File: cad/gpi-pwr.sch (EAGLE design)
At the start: 95 parts, among them CN1 HEADER-1X2, CN2 HEADER-3X1, CN3 HEADER-1X2.4, Q1 MOSFETTO247REV, Q3 MOSFETTO247REV, Q5 MOSFETTO247REV, Q6 MOSFETTO247REV, Q7 MOSFETTO247REV, Q8 MOSFETTO247REV, U1 ACS709, U2 ACS709, U3 ACPL-P346P346, U4 ACPL-P346P346, U5 ACPL-P346P346, U6 ACPL-P346P346, U7 ACPL-P346P346, U8 ACPL-P346P346

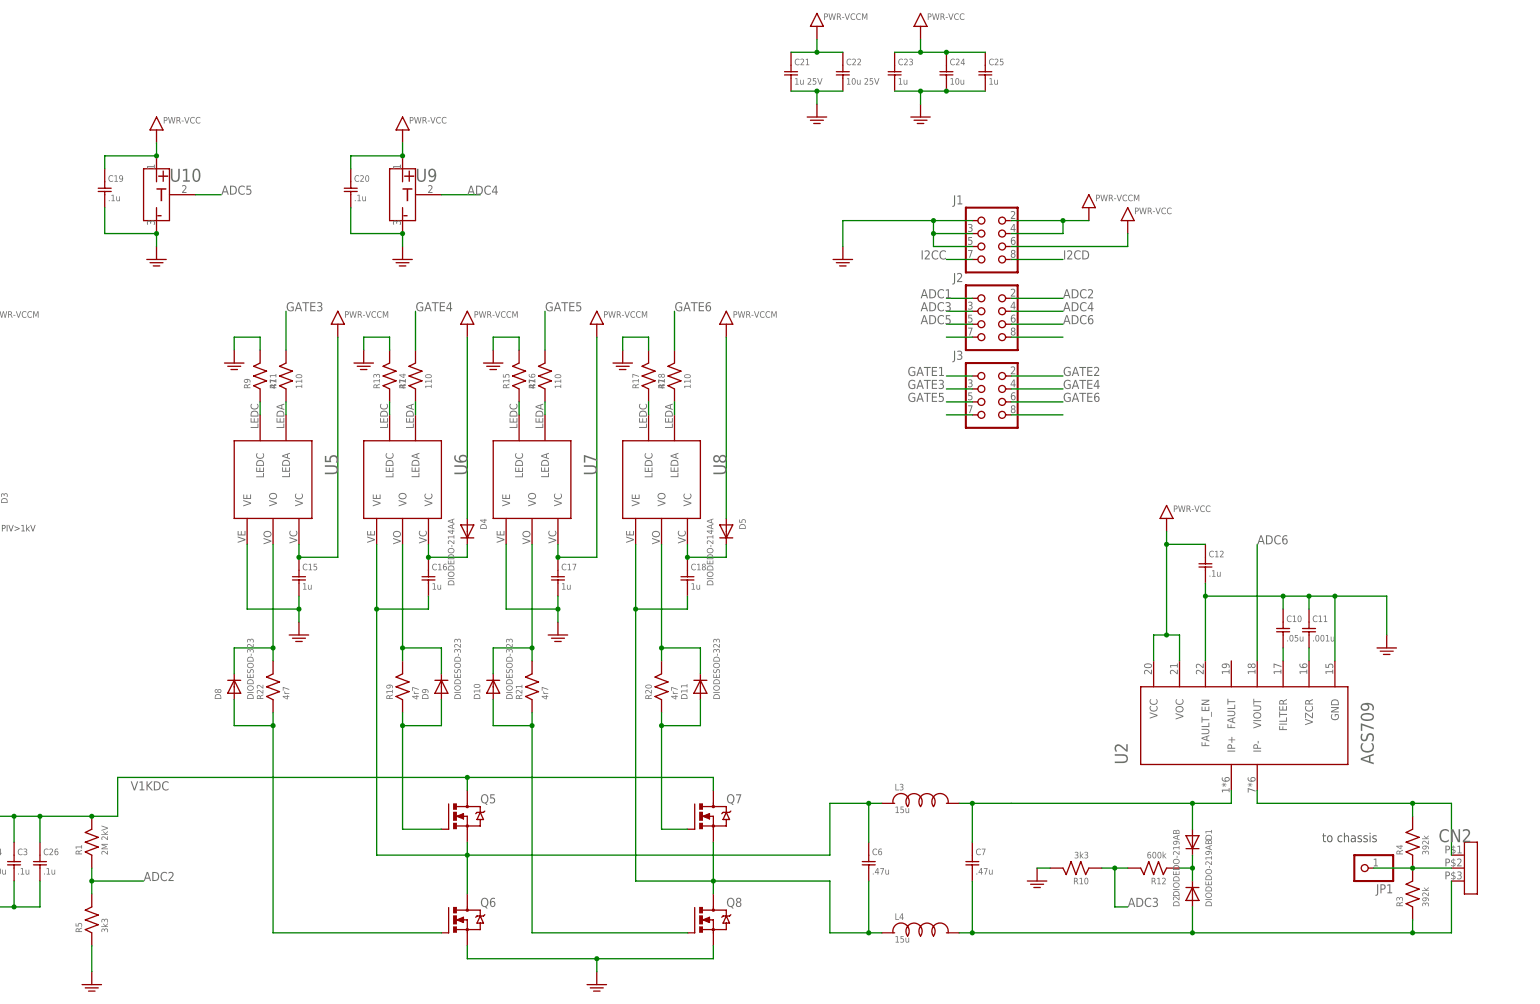
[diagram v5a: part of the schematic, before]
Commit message: op-amps on v-divs
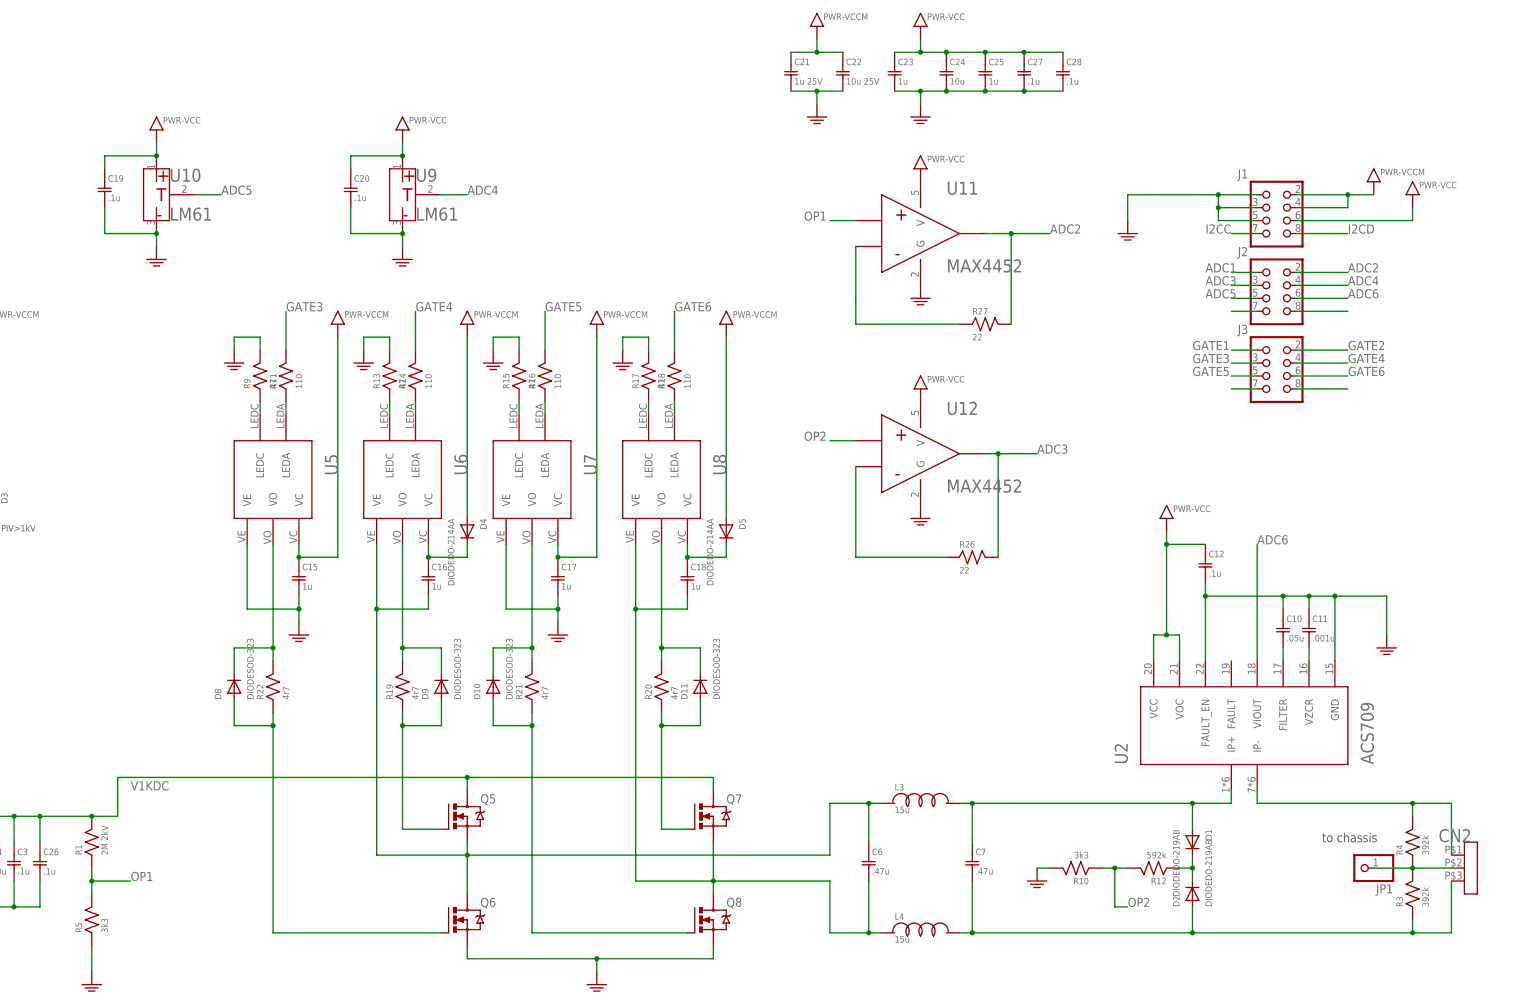
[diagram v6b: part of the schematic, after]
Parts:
- added C27, C28: .1u, jaw:C0603
- added R26, R27: 22, jaw:R0603
- added U11, U12: MAX4452, jaw:OPAMP
- R12: value 600k -> 592k
- U10, U9: value (none) -> LM61
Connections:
- new net N$51: R26.P$1, U12.INM
- new net N$52: R27.P$1, U11.INM
- new net OP1: R1.P$1, R5.P$2, U11.INP
- new net OP2: R10.P$1, R12.P$2, U12.INP
- net ADC2: now also R27.P$2, U11.OUT; no longer R1.P$1, R5.P$2
- net ADC3: now also R26.P$2, U12.OUT; no longer R10.P$1, R12.P$2
- net GND: now also C27.P$2, C28.P$2, U11.G, U12.G
- net VCC: now also C27.P$1, C28.P$1, U11.V, U12.V
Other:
- moved on the sheet: J1, J2, J3

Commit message: zoned grounds
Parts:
- added Z1: SHORT, jaw:SHORT
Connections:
- new net GNDA: C10.P$1, C11.P$1, C12.P$2, C19.P$2, C20.P$2, C23.P$2, C24.P$2, C25.P$2, C27.P$2, C28.P$2, C5.P$1, C8.P$1, C9.P$2, R10.P$2, R5.P$1, U1.FAULT_EN, U1.GND, U10.G, U11.G, U12.G, U2.FAULT_EN, U2.GND, U9.G, Z1.P$1
- new net GNDM: C13.P$2, C15.P$2, C17.P$2, C21.P$2, C22.P$2, J1.P$1, J1.P$3, J1.P$5, R13.P$2, R15.P$2, R17.P$2, R2.P$2, R7.P$2, R9.P$2, U3.VE, U5.VE, U7.VE, Z1.P$2
- net GND: no longer C10.P$1, C11.P$1, C12.P$2, C13.P$2, C15.P$2, C17.P$2, C19.P$2, C20.P$2, C21.P$2, C22.P$2, C23.P$2, C24.P$2, C25.P$2, C27.P$2, C28.P$2, C5.P$1, C8.P$1, C9.P$2, J1.P$1, J1.P$3, J1.P$5, R10.P$2, R13.P$2, R15.P$2, R17.P$2, R2.P$2, R5.P$1, R7.P$2, R9.P$2, U1.FAULT_EN, U1.GND, U10.G, U11.G, U12.G, U2.FAULT_EN, U2.GND, U3.VE, U5.VE, U7.VE, U9.G

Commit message: planes
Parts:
- removed Z1: SHORT, jaw:SHORT
- added C29, C30: .1u, jaw:C0603
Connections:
- removed net GNDA: C10.P$1, C11.P$1, C12.P$2, C19.P$2, C20.P$2, C23.P$2, C24.P$2, C25.P$2, C27.P$2, C28.P$2, C5.P$1, C8.P$1, C9.P$2, R10.P$2, R5.P$1, U1.FAULT_EN, U1.GND, U10.G, U11.G, U12.G, U2.FAULT_EN, U2.GND, U9.G, Z1.P$1
- removed net N$32: J2.P$7
- removed net N$45: J2.P$8
- removed net N$49: J3.P$8
- removed net N$53: J3.P$7
- net GNDM: now also C10.P$1, C11.P$1, C12.P$2, C19.P$2, C20.P$2, C23.P$2, C24.P$2, C25.P$2, C27.P$2, C28.P$2, C29.P$2, C30.P$2, C5.P$1, C8.P$1, C9.P$2, J2.P$7, J2.P$8, J3.P$7, J3.P$8, R10.P$2, R5.P$1, U1.FAULT_EN, U1.GND, U10.G, U11.G, U12.G, U2.FAULT_EN, U2.GND, U9.G; no longer Z1.P$2
- net VCC: now also C29.P$1, C30.P$1
